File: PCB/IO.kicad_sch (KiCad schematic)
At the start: 15 parts, among them J501 Conn_02x03_Counter_Clockwise, J502 USB_C_Receptacle_USB2.0_16P, J503 Screw_Terminal_01x06, J504 Screw_Terminal_01x04, J505 Conn_01x04, J506 Conn_02x03_Counter_Clockwise, J507 Conn_01x05

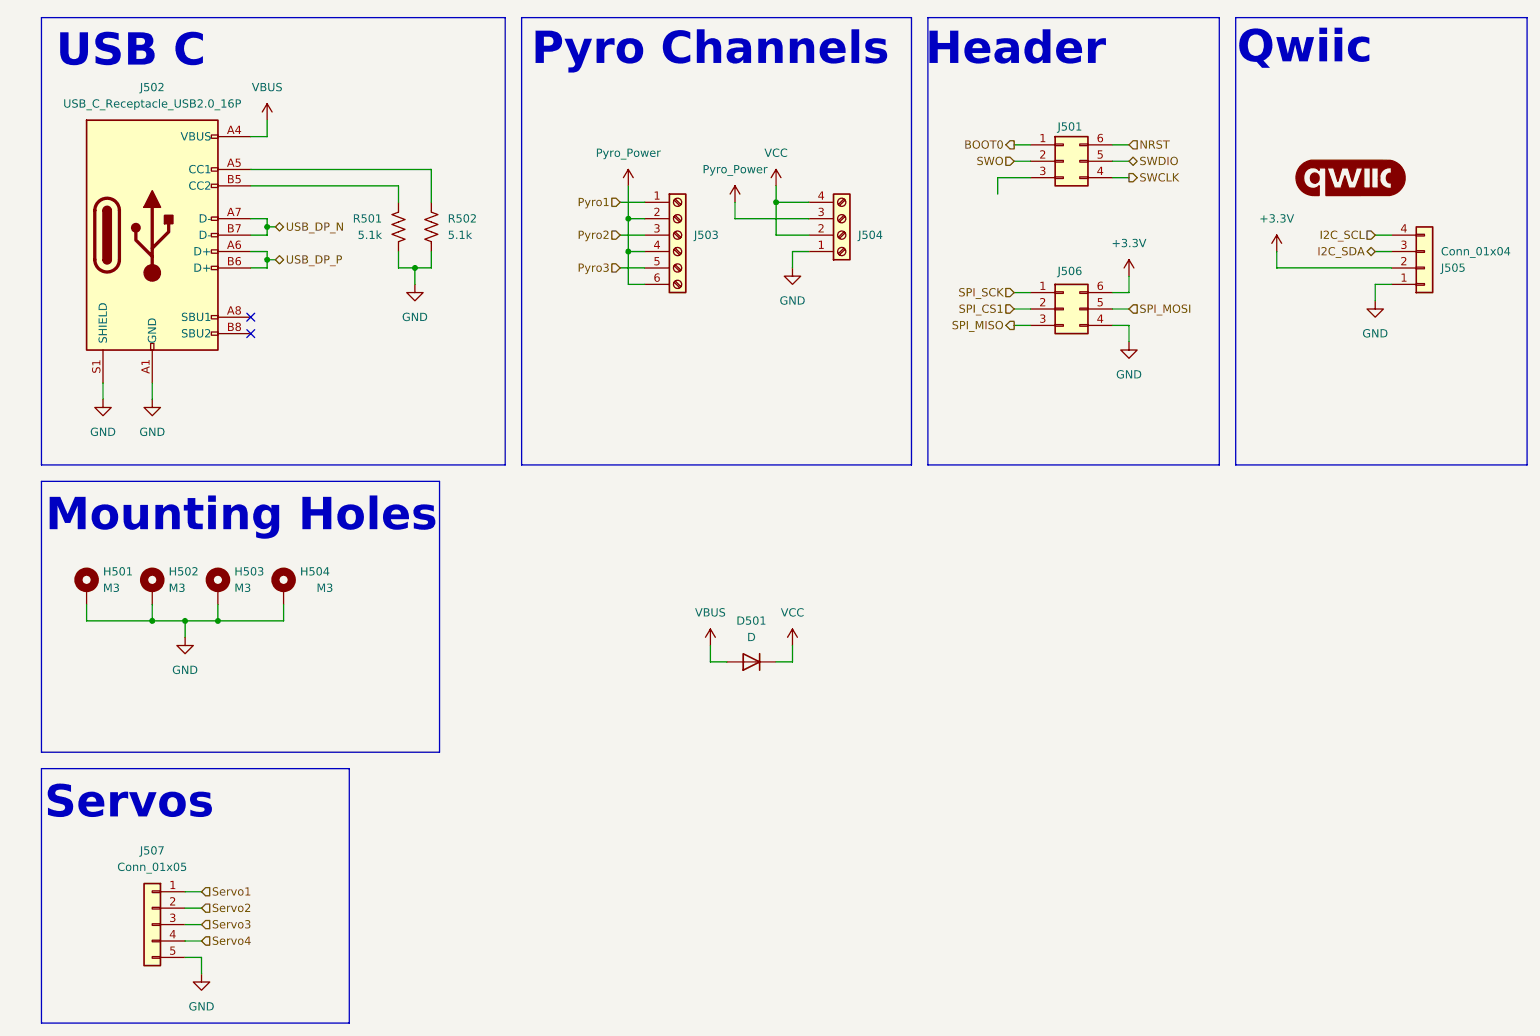
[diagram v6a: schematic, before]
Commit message: Added basic buzzer, LED, and fiducials to the schematic
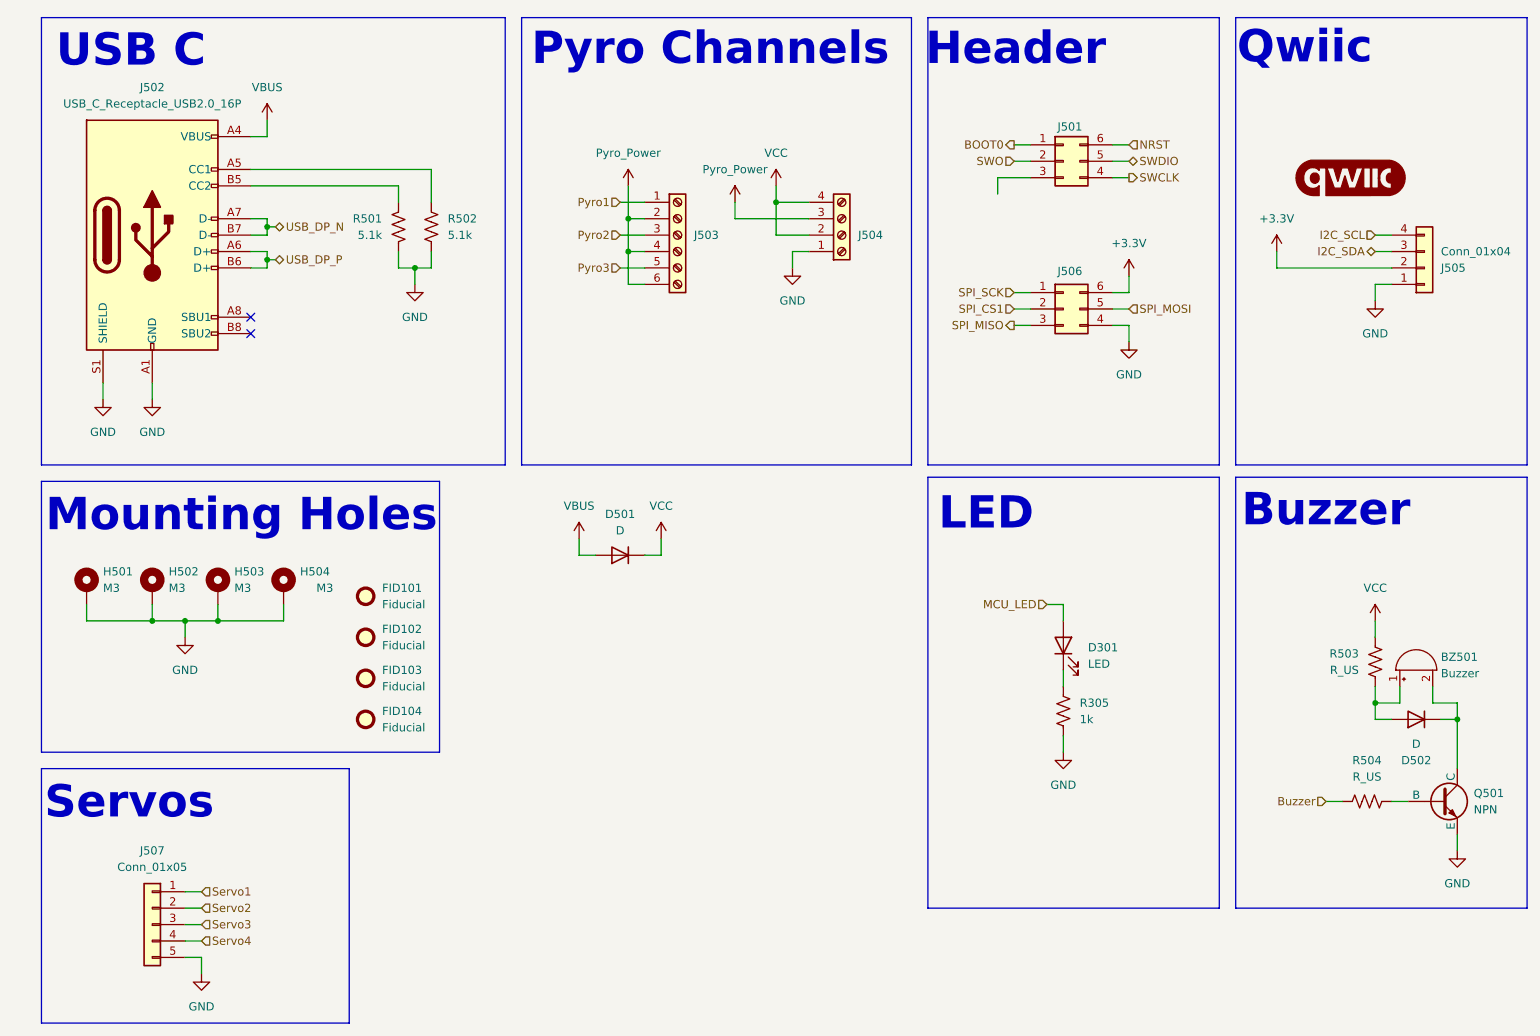
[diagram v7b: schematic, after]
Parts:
- added BZ501: Buzzer, symbol Device:Buzzer
- added D301: LED, LED_SMD:LED_0603_1608Metric_Pad1.05x0.95mm_HandSolder, symbol Device:LED
- added D502: D, symbol Device:D
- added FID101, FID102, FID103, FID104: Fiducial, Fiducial:Fiducial_0.75mm_Mask1.5mm, symbol Mechanical:Fiducial
- added Q501: NPN, symbol Simulation_SPICE:NPN
- added R305: 1k, Resistor_SMD:R_0603_1608Metric_Pad0.98x0.95mm_HandSolder, symbol Device:R_US
- added R503, R504: R_US, symbol Device:R_US
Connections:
- net GND: now also Q501.3 (E), R305.1
- net VCC: now also R503.1
- new net: BZ501.1 (+), D502.2 (A), R503.2
- new net: BZ501.2 (-), D502.1 (K), Q501.1 (C)
- new net: D301.1 (K), R305.2
- new net: Q501.2 (B), R504.2
- new net Buzzer: R504.1
- new net MCU_LED: D301.2 (A)
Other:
- note added: "Buzzer"
- note added: "LED"
- moved on the sheet: D501

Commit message: grounded programming interface
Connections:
- net GND: now also J501.3 (Pin_3)
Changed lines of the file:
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@@
 	(wire
 		(pts
-			(xy 162.56 39.37) (xy 162.56 41.91)
+			(xy 165.1 39.37) (xy 165.1 41.91)
 		)
 		(stroke
@@
 	(wire
 		(pts
-			(xy 162.56 39.37) (xy 167.64 39.37)
+			(xy 165.1 39.37) (xy 167.64 39.37)
 		)
 		(stroke
@@
 					(unit 1)
 				)
+			)
+		)
+	)
+	(symbol
+		(lib_id "power:GND")
+		(at 165.1 41.91 0)
+		(unit 1)
+		(exclude_from_sim no)
+		(in_bom yes)
+		(on_board yes)
+		(dnp no)
+		(property "Reference" "#PWR01"
+			(at 165.1 48.26 0)
+			(effects
+				(font
+					(size 1.27 1.27)
+				)
+				(hide yes)
+			)
+		)
+		(property "Value" "GND"
+			(at 165.1 46.99 0)
+			(effects
+				(font
+					(size 1.27 1.27)
+				)
+			)
+		)
+		(property "Footprint" ""
+			(at 165.1 41.91 0)
+			(effects
+				(font
+					(size 1.27 1.27)
+				)
+				(hide yes)
+			)
+		)
+		(property "Datasheet" ""
+			(at 165.1 41.91 0)
+			(effects
+				(font
+					(size 1.27 1.27)
+				)
+				(hide yes)
+			)
+		)
+		(property "Description" "Power symbol creates a global label with name \"GND\" , ground"
+			(at 165.1 41.91 0)
+			(effects
+				(font
+					(size 1.27 1.27)
+				)
+				(hide yes)
+			)
+		)
+		(pin "1"
+		)
+		(instances
+			(project "Flight Computer"
+				(path "/4254ccd1-49f4-4fe6-9bf7-ccb200d73af4/0a0b3d01-7422-42e0-b725-ff9e85b891ec"
+					(reference "#PWR01")
+					(unit 1)
+				)
